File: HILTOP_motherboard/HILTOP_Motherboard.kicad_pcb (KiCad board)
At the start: 4 copper layers, 170 x 170 mm, 709 parts, among them J1 BACKPLANE_PWR, J10 HDMI, J11 DISP_PWR, J12 DISPLAY_PORT, J13 DDR2_SODIMM_COMPUTE_MODULE_3, J14 VADJ_B, J15 VADJ_A, J16 SOFT_START_PWR, J17 PWR_LED, J18 USB_B, J19 Micro_SD_Card, J2 ATX_MOLEX_02X12, J20 CAMERA_PORT, J21 EXT_FAN, J22 BACKPLANE_LV_PWR, J23 EXT_FAN, J24 HILTOP_PCIE-64_CONN, J25 DEBUG, J3 SATA, J4 USB_A_DOUBLE, J5 USB Front Panel, J6 Conn_02x05_Odd_Even, J7 Conn_02x08_Odd_Even, J8 EXT_TEMP_MON, J9 RJ45-TRANS_SI-61001-F, Q1 Q_NMOS_DS_POWERPAK, Q2 Q_NMOS_DS_POWERPAK, Q3 2N7002, Q4 2N7002, Q5 ZXMN6A07F, Q6 ZXMN6A07F, U1 LM337BD2TG, U10 TLC271, U11 ADS1015, U12 MCP4725, U13 AM1S-0505SZ, U14 SP3003-02XJ, U15 ISO3080, U16 ISO3080, U17 AM1S-0505SZ, U18 USB6B1, U19 USB6B1, U2 MIC2026-1YM, U20 USB6B1, U21 USB6B1, U22 BQ32000, U23 TPD12S016, U24 MAX16054, U25 STM6719SFWB6F, U26 LM75B, U27 TPS54394, U28 LP2985, U29 AM1S-0505SZ, U3 USB2517, U30 MCP2517FD, U31 MCP2517FD, U32 AM1S-0505SZ, U33 ADuM1201, U34 ADuM1201, U35 MCP2561FD, U36 MCP2561FD, U37 TUSB9261, U38 AT25DN512CSSHF-B, U39 MCP23017, U4 MIC2026-1YM, U40 SP3003-02XJ, U41 CP2102N-A01-GQFN24, U42 FDC6330L, U43 MAX3107, U44 MAX3107, U45 93AAxxA, U5 SP3003-02XJ, U6 SP3003-02XJ, U7 LAN7500, U8 LM5118, U9 INA250A3, Y1 24MHz Crystal, Y2 25MHz Crystal, Y3 0.22F, Y4 32.768kHz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

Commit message: BOM nearly complete!
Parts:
- removed D66, D67, D69, D70, D71, D72, D73, D77, D78, D79, D80, D81, D82, D83: BAV99, Package_TO_SOT_SMD:SOT-23
- removed R184, R185, R186, R187, R188, R192, R193, R194, R195, R196, R197, R198: 220R, Resistor_SMD:R_0603_1608Metric
- removed R206, R207: 2K2, Resistor_SMD:R_0603_1608Metric
- added D34: BAV99, Package_TO_SOT_SMD:SOT-23, B.Cu at (179.7, 104.2)
- added D35: BAV99, Package_TO_SOT_SMD:SOT-23, B.Cu at (181.6, 100.5)
- added D93: BAV99, Package_TO_SOT_SMD:SOT-23, B.Cu at (176.0, 104.2)
- added D94: BAV99, Package_TO_SOT_SMD:SOT-23, B.Cu at (172.2, 104.2)
- added D95: BAV99, Package_TO_SOT_SMD:SOT-23, B.Cu at (174.1, 100.5)
- added D96: BAV99, Package_TO_SOT_SMD:SOT-23, B.Cu at (177.8, 100.5)
- added J26: Conn_02x06_Odd_Even, Connector_IDC:IDC-Header_2x06_P2.54mm_Vertical, F.Cu at (187.2, 126.8)
- added R245: 220R, Resistor_SMD:R_0402_1005Metric, B.Cu at (181.6, 107.5)
- added R246: 220R, Resistor_SMD:R_0402_1005Metric, B.Cu at (179.9, 107.6)
- added R247: 220R, Resistor_SMD:R_0402_1005Metric, B.Cu at (178.1, 107.8)
- added R248: 220R, Resistor_SMD:R_0402_1005Metric, B.Cu at (176.3, 108.3)
- added R249: 220R, Resistor_SMD:R_0402_1005Metric, B.Cu at (174.1, 108.2)
- added TP17: TP, TestPoint:TestPoint_THTPad_D1.0mm_Drill0.5mm, F.Cu at (232.5, 176.9)
- added TP18: TP, TestPoint:TestPoint_THTPad_D1.0mm_Drill0.5mm, F.Cu at (228.4, 168.7)
- added TP19: TP, TestPoint:TestPoint_THTPad_D1.0mm_Drill0.5mm, F.Cu at (230.5, 166.6)
- added TP20: TP, TestPoint:TestPoint_THTPad_D1.0mm_Drill0.5mm, F.Cu at (228.4, 170.7)
- added TP21: TP, TestPoint:TestPoint_THTPad_D1.0mm_Drill0.5mm, F.Cu at (230.5, 168.7)
- added TP22: TP, TestPoint:TestPoint_THTPad_D1.0mm_Drill0.5mm, F.Cu at (232.5, 166.6)
- added TP23: TP, TestPoint:TestPoint_THTPad_D1.0mm_Drill0.5mm, F.Cu at (228.4, 172.8)
- added TP24: TP, TestPoint:TestPoint_THTPad_D1.0mm_Drill0.5mm, F.Cu at (230.5, 170.7)
- added TP25: TP, TestPoint:TestPoint_THTPad_D1.0mm_Drill0.5mm, F.Cu at (232.5, 168.7)
- added TP26: TP, TestPoint:TestPoint_THTPad_D1.0mm_Drill0.5mm, F.Cu at (234.6, 166.6)
- added TP27: TP, TestPoint:TestPoint_THTPad_D1.0mm_Drill0.5mm, F.Cu at (234.6, 174.8)
- added TP28: TP, TestPoint:TestPoint_THTPad_D1.0mm_Drill0.5mm, F.Cu at (230.5, 172.8)
- added TP29: TP, TestPoint:TestPoint_THTPad_D1.0mm_Drill0.5mm, F.Cu at (232.5, 170.7)
- added TP30: TP, TestPoint:TestPoint_THTPad_D1.0mm_Drill0.5mm, F.Cu at (234.6, 168.7)
- added TP31: TP, TestPoint:TestPoint_THTPad_D1.0mm_Drill0.5mm, F.Cu at (236.6, 166.6)
- added TP32: TP, TestPoint:TestPoint_THTPad_D1.0mm_Drill0.5mm, F.Cu at (228.4, 176.9)
- added TP33: TP, TestPoint:TestPoint_THTPad_D1.0mm_Drill0.5mm, F.Cu at (230.5, 174.8)
- added TP34: TP, TestPoint:TestPoint_THTPad_D1.0mm_Drill0.5mm, F.Cu at (232.5, 172.8)
- added TP35: TP, TestPoint:TestPoint_THTPad_D1.0mm_Drill0.5mm, F.Cu at (234.6, 170.7)
- added TP36: TP, TestPoint:TestPoint_THTPad_D1.0mm_Drill0.5mm, F.Cu at (236.6, 168.7)
- added TP37: TP, TestPoint:TestPoint_THTPad_D1.0mm_Drill0.5mm, F.Cu at (228.4, 166.6)
- added TP38: TP, TestPoint:TestPoint_THTPad_D1.0mm_Drill0.5mm, F.Cu at (228.4, 178.9)
- added TP39: TP, TestPoint:TestPoint_THTPad_D1.0mm_Drill0.5mm, F.Cu at (230.5, 176.9)
- added TP40: TP, TestPoint:TestPoint_THTPad_D1.0mm_Drill0.5mm, F.Cu at (232.5, 174.8)
- added TP41: TP, TestPoint:TestPoint_THTPad_D1.0mm_Drill0.5mm, F.Cu at (234.6, 172.8)
- added TP42: TP, TestPoint:TestPoint_THTPad_D1.0mm_Drill0.5mm, F.Cu at (236.6, 170.7)
- added TP43: TP, TestPoint:TestPoint_THTPad_D1.0mm_Drill0.5mm, F.Cu at (238.7, 168.7)
- added TP44: TP, TestPoint:TestPoint_THTPad_D1.0mm_Drill0.5mm, F.Cu at (240.7, 166.6)
- added TP45: TP, TestPoint:TestPoint_THTPad_D1.0mm_Drill0.5mm, F.Cu at (230.5, 178.9)
- added TP46: TP, TestPoint:TestPoint_THTPad_D1.0mm_Drill0.5mm, F.Cu at (228.4, 174.8)
- added TP47: TP, TestPoint:TestPoint_THTPad_D1.0mm_Drill0.5mm, F.Cu at (238.7, 166.6)
- added TP48: TP, TestPoint:TestPoint_THTPad_D1.0mm_Drill0.5mm, F.Cu at (236.6, 172.8)
- added TP49: TP, TestPoint:TestPoint_THTPad_D1.0mm_Drill0.5mm, F.Cu at (238.7, 170.7)
- added TP50: TP, TestPoint:TestPoint_THTPad_D1.0mm_Drill0.5mm, F.Cu at (240.7, 168.7)
- added TP51: TP, TestPoint:TestPoint_THTPad_D1.0mm_Drill0.5mm, F.Cu at (242.8, 166.6)
- added TP52: TP, TestPoint:TestPoint_THTPad_D1.0mm_Drill0.5mm, F.Cu at (232.5, 178.9)
- added TP53: TP, TestPoint:TestPoint_THTPad_D1.0mm_Drill0.5mm, F.Cu at (234.6, 176.9)
- added TP54: TP, TestPoint:TestPoint_THTPad_D1.0mm_Drill0.5mm, F.Cu at (236.6, 174.8)
- added TP55: TP, TestPoint:TestPoint_THTPad_D1.0mm_Drill0.5mm, F.Cu at (238.7, 172.8)
- added TP56: TP, TestPoint:TestPoint_THTPad_D1.0mm_Drill0.5mm, F.Cu at (251.0, 168.7)
- added TP57: TP, TestPoint:TestPoint_THTPad_D1.0mm_Drill0.5mm, F.Cu at (242.8, 168.7)
- added TP58: TP, TestPoint:TestPoint_THTPad_D1.0mm_Drill0.5mm, F.Cu at (244.8, 166.6)
- added TP59: TP, TestPoint:TestPoint_THTPad_D1.0mm_Drill0.5mm, F.Cu at (234.6, 178.9)
- added TP60: TP, TestPoint:TestPoint_THTPad_D1.0mm_Drill0.5mm, F.Cu at (236.6, 176.9)
- added TP61: TP, TestPoint:TestPoint_THTPad_D1.0mm_Drill0.5mm, F.Cu at (238.7, 174.8)
- added TP62: TP, TestPoint:TestPoint_THTPad_D1.0mm_Drill0.5mm, F.Cu at (240.7, 172.8)
- added TP63: TP, TestPoint:TestPoint_THTPad_D1.0mm_Drill0.5mm, F.Cu at (242.8, 170.7)
- added TP64: TP, TestPoint:TestPoint_THTPad_D1.0mm_Drill0.5mm, F.Cu at (244.8, 168.7)
- added TP65: TP, TestPoint:TestPoint_THTPad_D1.0mm_Drill0.5mm, F.Cu at (246.9, 166.6)
- added TP66: TP, TestPoint:TestPoint_THTPad_D1.0mm_Drill0.5mm, F.Cu at (242.8, 178.9)
- added TP67: TP, TestPoint:TestPoint_THTPad_D1.0mm_Drill0.5mm, F.Cu at (238.7, 176.9)
- added TP68: TP, TestPoint:TestPoint_THTPad_D1.0mm_Drill0.5mm, F.Cu at (240.7, 174.8)
- added TP69: TP, TestPoint:TestPoint_THTPad_D1.0mm_Drill0.5mm, F.Cu at (242.8, 172.8)
- added TP70: TP, TestPoint:TestPoint_THTPad_D1.0mm_Drill0.5mm, F.Cu at (244.8, 170.7)
- added TP71: TP, TestPoint:TestPoint_THTPad_D1.0mm_Drill0.5mm, F.Cu at (246.9, 168.7)
- added TP72: TP, TestPoint:TestPoint_THTPad_D1.0mm_Drill0.5mm, F.Cu at (248.9, 166.6)
- added TP73: TP, TestPoint:TestPoint_THTPad_D1.0mm_Drill0.5mm, F.Cu at (238.7, 178.9)
- added TP74: TP, TestPoint:TestPoint_THTPad_D1.0mm_Drill0.5mm, F.Cu at (240.7, 176.9)
- added TP75: TP, TestPoint:TestPoint_THTPad_D1.0mm_Drill0.5mm, F.Cu at (242.8, 174.8)
- added TP76: TP, TestPoint:TestPoint_THTPad_D1.0mm_Drill0.5mm, F.Cu at (240.7, 170.7)
- added TP77: TP, TestPoint:TestPoint_THTPad_D1.0mm_Drill0.5mm, F.Cu at (246.9, 170.7)
- added TP78: TP, TestPoint:TestPoint_THTPad_D1.0mm_Drill0.5mm, F.Cu at (248.9, 168.7)
- added TP79: TP, TestPoint:TestPoint_THTPad_D1.0mm_Drill0.5mm, F.Cu at (251.0, 166.6)
- added TP80: TP, TestPoint:TestPoint_THTPad_D1.0mm_Drill0.5mm, F.Cu at (240.7, 178.9)
- added TP81: TP, TestPoint:TestPoint_THTPad_D1.0mm_Drill0.5mm, F.Cu at (242.8, 176.9)
- added TP82: TP, TestPoint:TestPoint_THTPad_D1.0mm_Drill0.5mm, F.Cu at (244.8, 174.8)
- added TP83: TP, TestPoint:TestPoint_THTPad_D1.0mm_Drill0.5mm, F.Cu at (246.9, 172.8)
- added TP84: TP, TestPoint:TestPoint_THTPad_D1.0mm_Drill0.5mm, F.Cu at (248.9, 170.7)
- added TP85: TP, TestPoint:TestPoint_THTPad_D1.0mm_Drill0.5mm, F.Cu at (236.6, 178.9)
- added TP86: TP, TestPoint:TestPoint_THTPad_D1.0mm_Drill0.5mm, F.Cu at (244.8, 172.8)
- added TP87: TP, TestPoint:TestPoint_THTPad_D1.0mm_Drill0.5mm, F.Cu at (244.8, 176.9)
- added TP88: TP, TestPoint:TestPoint_THTPad_D1.0mm_Drill0.5mm, F.Cu at (246.9, 174.8)
- added TP89: TP, TestPoint:TestPoint_THTPad_D1.0mm_Drill0.5mm, F.Cu at (248.9, 172.8)
- added TP90: TP, TestPoint:TestPoint_THTPad_D1.0mm_Drill0.5mm, F.Cu at (251.0, 170.7)
- added TP91: TP, TestPoint:TestPoint_THTPad_D1.0mm_Drill0.5mm, F.Cu at (244.8, 178.9)
- added TP92: TP, TestPoint:TestPoint_THTPad_D1.0mm_Drill0.5mm, F.Cu at (246.9, 176.9)
- added TP93: TP, TestPoint:TestPoint_THTPad_D1.0mm_Drill0.5mm, F.Cu at (248.9, 174.8)
- added TP94: TP, TestPoint:TestPoint_THTPad_D1.0mm_Drill0.5mm, F.Cu at (251.0, 172.8)
- C113, C222, C223, C77, D38, D39, D40, D41, D84, FB11, FB7, Q5, Q6, R10, R167, R2, R210, R211, R212, R213, R214, R215, R216, R217, R218, R24, R3, R91, U2, U39, U4, U40, U41, U42: moved to B.Cu
- C18: moved to F.Cu
- D11, D12, D13, D14, D15, D16, D17, D2, D3, D4, D85, D86, D87, D88, D89, D90, D91, D92: footprint LED_SMD:LED_0603_1608Metric -> LED_SMD:LED_0402_1005Metric
- EXP1, EXP2, EXP3: footprint Connector_PinHeader_2.54mm:PinHeader_2x20_P2.54mm_Vertical -> Connector_IDC:IDC-Header_2x20_P2.54mm_Vertical
- J12, J20: footprint Devtank_PCB_Lib:DSI_SFW15R-2STE1LF -> Devtank_PCB_Lib:DSI_FCC15W_VERT
- R140, R141, R153, R154, R155, R156, R157, R158, R182, R183, R189, R190, R191, R235, R236, R237, R238, R239, R240, R241, R242, R28, R35, R36, R37, R38, R39, R40, R41, R42, R43, R44, R45, R46, R47, R48, R80, R82, R84, R86, R87, R88, R89, R90, R92, R93, R94, R95, R96, R97: footprint Resistor_SMD:R_0603_1608Metric -> Resistor_SMD:R_0402_1005Metric
- R178, R179, R180, R181: footprint Resistor_SMD:R_0603_1608Metric -> Resistor_SMD:R_0402_1005Metric; moved to B.Cu
- R54: value DNF -> 220R; footprint Resistor_SMD:R_0603_1608Metric -> Resistor_SMD:R_0402_1005Metric; moved to B.Cu
- moved C21 308.8 mm to (243.5, 107.4)
- moved C28 308.8 mm to (246.2, 111.5)
- moved C32 308.8 mm to (246.2, 112.2)
- moved C35 308.8 mm to (250.6, 108.4)
- moved C37 308.8 mm to (246.2, 113.0)
- moved C39 308.8 mm to (244.6, 114.6)
- moved C40 308.8 mm to (250.6, 109.1)
- moved D11 308.8 mm to (231.8, 114.7)
- moved D12 308.8 mm to (231.8, 111.5)
- moved D13 308.8 mm to (228.8, 114.7)
- moved D14 308.8 mm to (240.5, 104.3)
- moved D15 308.8 mm to (228.8, 113.1)
- moved D16 308.8 mm to (237.4, 105.9)
- moved D17 308.8 mm to (237.4, 104.3)
- moved D2 308.8 mm to (234.9, 111.5)
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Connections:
- J13 pad 30: /Processor/GPIO29 -> /SYS_FAN_DC
- J13 pad 34: /Processor/GPIO30 -> /EXT_TEMP_1WIRE
- J13 pad 36: /Processor/GPIO31 -> /BCK_SHUTDOWN
- J13 pad 46: /Processor/GPIO32 -> /FAN_SENSE_2
- J13 pad 48: /Processor/GPIO33 -> /FAN_SENSE_1
- J13 pad 60: /Processor/GPIO37 -> /DC_DC_ENABLE
- J13 pad 64: /Processor/GPIO38 -> /UART_CH1_CS
- J13 pad 66: /Processor/GPIO39 -> /UART_CH2_CS
- J13 pad 70: /Processor/GPIO40 -> /CAN_CH1_CS
- J13 pad 72: /Processor/GPIO41 -> /CAN_CH2_CS
- J13 pad 76: /Processor/GPIO42 -> /MCP23017_INTA
- J13 pad 78: /Processor/GPIO43 -> /MCP23017_INTB
- J13 pad 82: Net-(D66-Pad3) -> /DC_OUT_ENABLE
- J13 pad 84: Net-(D67-Pad3) -> /ATX_PWR_SHDN
- J2 pad 20: Net-(J2-Pad20) -> (no net)
- Q3 pad 1: (no net) -> Net-(Q3-Pad1)
- R100 pad 1: Net-(D67-Pad3) -> /ATX_PWR_SHDN
- R101 pad 1: Net-(D66-Pad3) -> /DC_OUT_ENABLE
- R108 pad 1: Net-(R108-Pad1) -> Net-(Q3-Pad1)
- R110 pad 2: Net-(R108-Pad1) -> Net-(Q3-Pad1)
- R54 pad 1: Net-(C119-Pad2) -> Net-(J26-Pad1)
- R54 pad 2: Net-(J2-Pad20) -> /EXT_GPIO1
- R99 pad 1: /Processor/GPIO29 -> /SYS_FAN_DC
- U30 pad 8: (no net) -> /CAN2_INT1
- U30 pad 9: (no net) -> /CAN2_INT0
- U31 pad 8: (no net) -> /CAN1_INT1
- U31 pad 9: (no net) -> /CAN1_INT0
- U39 pad 23: (no net) -> /EXT_GPIO1
- U39 pad 24: (no net) -> /EXT_GPIO2
- U39 pad 25: (no net) -> /EXT_GPIO3
- U39 pad 26: (no net) -> /EXT_GPIO4
- U39 pad 27: (no net) -> /EXT_GPIO5
- U39 pad 28: (no net) -> /EXT_GPIO6
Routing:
- net +1V8: track 124.2 -> 36.5 mm, vias 2 -> 1
- net Net-(J2-Pad20): track 33.2 -> 0.00 mm
- net +CM_1V8: track 40.3 -> 21.2 mm
- net /AdjPower/VADJ_DC: track 0.00 -> 17.2 mm
- net ADJ_DC: track 0.00 -> 15.2 mm
- net Net-(C113-Pad1): track 15.0 -> 0.90 mm
- net /Processor/HDMI_SDA: track 18.0 -> 5.82 mm, vias 1 -> 0
- net /Processor/HDMI_HPD: track 17.7 -> 5.71 mm
- net /Processor/GPIO4: track 9.29 -> 0.00 mm, vias 1 -> 0
- net /Processor/SDX_D2: track 27.9 -> 19.2 mm
- net /Processor/SDX_D0: track 27.5 -> 19.0 mm, vias 2 -> 0
- net /Processor/SDX_D1: track 27.2 -> 18.6 mm, vias 2 -> 0
- net /Processor/SDX_CLK: track 27.5 -> 19.0 mm
- net /Processor/SDX_D3: track 27.4 -> 18.9 mm, vias 2 -> 0
- net /Processor/SDX_CMD: track 27.5 -> 19.7 mm
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- added copper zone on F.Cu, net Net-(C50-Pad2)
- removed copper zone on In2.Cu, net ADJ_DC
- removed copper zone on In1.Cu, net GND
- removed copper zone on In2.Cu, net GND_ISO4
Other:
- copper layers 4 -> 6

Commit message: nearly finished placing all parts!
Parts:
- removed C53, C55: 100nF, Capacitor_SMD:C_0201_0603Metric
- removed C59, C71, C72, C73: 100nF, Capacitor_SMD:C_0603_1608Metric
- removed D52, D53: BAV99, Package_TO_SOT_SMD:SOT-23
- removed EXP3: CONN_02X20, Connector_IDC:IDC-Header_2x20_P2.54mm_Vertical
- removed R210, R213: 100K, Resistor_SMD:R_0603_1608Metric
- removed R211: DNP, Resistor_SMD:R_0603_1608Metric
- removed R212, R214: 1K, Resistor_SMD:R_0603_1608Metric
- removed R93, R94: 220R, Resistor_SMD:R_0402_1005Metric
- removed U42: FDC6330L, Devtank_PCB_Lib:SuperSOT-6
- removed W1: TP, TestPoint:TestPoint_THTPad_1.5x1.5mm_Drill0.7mm
- removed Y3: 0.22F, Devtank_PCB_Lib:Battery_SD_V_SuperCap
- added BT1: Battery_Cell, Devtank_PCB_Lib:BatteryHolder_Keystone_1061_1x20mm, F.Cu at (155.1, 155.9)
- added C237: DNF, Capacitor_SMD:C_0603_1608Metric, F.Cu at (211.9, 89.5)
- added C238: DNF, Capacitor_SMD:C_0603_1608Metric, F.Cu at (215.7, 92.8)
- added D66: MBR230LSFT, Diode_SMD:D_SOD-123F, F.Cu at (154.2, 157.8)
- added Q7: ZXMN6A07F, Package_TO_SOT_SMD:SOT-23, F.Cu at (206.2, 88.9)
- added Q8: SSM3J328R, Package_TO_SOT_SMD:SOT-23, F.Cu at (211.8, 94.8)
- added R184: 10K, Resistor_SMD:R_0603_1608Metric, F.Cu at (211.9, 91.7)
- added R185: 10K, Resistor_SMD:R_0603_1608Metric, F.Cu at (206.3, 85.0)
- added TP95: TP, TestPoint:TestPoint_THTPad_D1.0mm_Drill0.5mm, F.Cu at (197.4, 178.2)
- C100, C101, C102, C15, C153, C154, C181, C182, C183, C195, C196, C20, C201, C202, C203, C205, C207, C209, C211, C212, C213, C214, C215, C216, C217, C218, C220, C221, C224, C43, C45, C46, C65, C76, C84, D42, D43, D44, D45, D46, D47, D48, D49, D50, D51, D54, D55, D59, D60, D61, D62, D63, D64, D65, R11, R18, R182, R19: moved to B.Cu
- C197, C198, C199, C200: footprint Resistor_SMD:R_0402_1005Metric -> Capacitor_SMD:C_0402_1005Metric
- C47, C48, C49: footprint Resistor_SMD:R_0603_1608Metric -> Capacitor_SMD:C_0603_1608Metric
- D1, D21, D22, D23: value Green_LED -> GRN; footprint LED_SMD:LED_0603_1608Metric -> LED_SMD:LED_0402_1005Metric
- D18: value Green_LED -> GRN; footprint LEDs:LED_0603 -> LED_SMD:LED_0402_1005Metric
- D25, D26, D27, D28, D29, D30, D31, D32, D33: footprint LED_SMD:LED_0603_1608Metric -> LED_SMD:LED_0402_1005Metric
- D84, R167, U41: moved to F.Cu
- F1: value PPTC 2A, 3.8A, 32V -> PPTC 3.8A
- J26: value Conn_02x06_Odd_Even -> IO_EXP
- J5: value USB Front Panel -> USB FRONT PANEL
- J6: value Conn_02x05_Odd_Even -> CAN
- J7: value Conn_02x08_Odd_Even -> RS485
- L11, L5, L6, L7: value 15uH -> 10uH
- Q1, Q2: value Q_NMOS_DS_POWERPAK -> Si7148DP-T1-E3
- R100, R101, R102, R31, R32, R33, R99: footprint Resistor_SMD:R_0603_1608Metric -> Resistor_SMD:R_0402_1005Metric
- R159: value 0R -> 10K
- TP15, TP16: value Test_Point -> TP
- U13, U17, U29, U32: value AM1S-0505SZ -> CME0505S3C
- U39: footprint Package_SO:SOIC-28W_7.5x17.9mm_P1.27mm -> Package_SO:SSOP-28_5.3x10.2mm_P0.65mm
- moved R95 240.5 mm to (191.8, 102.2), turned to 270 degrees
- moved R97 236.5 mm to (190.4, 102.2), turned to 270 degrees
- moved R92 235.6 mm to (195.0, 95.8)
- moved C224 231.0 mm to (182.3, 65.5)
- moved R96 228.8 mm to (189.0, 102.2), turned to 90 degrees
- moved C225 228.7 mm to (183.2, 65.4)
- moved C217 227.2 mm to (178.5, 66.5), turned to 180 degrees
- moved R140 227.0 mm to (187.6, 102.2), turned to 270 degrees
- moved R141 225.7 mm to (182.0, 102.2), turned to 270 degrees
- moved R86 224.5 mm to (183.4, 102.2), turned to 270 degrees
- moved R156 223.9 mm to (171.3, 102.2), turned to 270 degrees
- moved R153 223.3 mm to (186.2, 102.2), turned to 90 degrees
- moved R84 223.0 mm to (184.8, 102.2), turned to 270 degrees
- moved R87 222.7 mm to (179.2, 102.2), turned to 270 degrees
- moved C219 221.1 mm to (178.8, 67.0), turned to 180 degrees
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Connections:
- C102 pad 2: Net-(C102-Pad2) -> +5V
- C15 pad 2: GND -> GND_ISO3
- C20 pad 2: GND -> GND_ISO4
- C44 pad 2: Net-(C44-Pad2) -> +5V
- C78 pad 2: Net-(C78-Pad2) -> +5V
- C84 pad 2: Net-(C84-Pad2) -> +5V
- FL1 pad 1: Net-(C161-Pad1) -> Net-(C158-Pad1)
- FL1 pad 2: /CAN2_H -> Net-(C161-Pad1)
- FL1 pad 3: Net-(C158-Pad1) -> /CAN2_H
- FL2 pad 1: Net-(C162-Pad1) -> Net-(C159-Pad1)
- FL2 pad 2: /CAN1_H -> Net-(C162-Pad1)
- FL2 pad 3: Net-(C159-Pad1) -> /CAN1_H
- J13 pad 51: /Processor/GPIO14 -> /DEBUG_TX
- J13 pad 53: /Processor/GPIO15 -> /DEBUG_RX
- L11 pad 1: +5V -> Net-(L11-Pad1)
- L11 pad 2: Net-(C102-Pad2) -> +5V_ISO2
- L5 pad 1: +5V -> Net-(L5-Pad1)
- L5 pad 2: Net-(C78-Pad2) -> +5V_ISO3
- L6 pad 1: +5V -> Net-(L6-Pad1)
- L6 pad 2: Net-(C44-Pad2) -> +5V_ISO4
- L7 pad 1: +5V -> Net-(L7-Pad1)
- L7 pad 2: Net-(C84-Pad2) -> +5V_ISO1
- R159 pad 1: Net-(R159-Pad1) -> /SYS_FAN_DC
- R159 pad 2: Net-(R159-Pad2) -> GND
- TP35 pad 1: /CAN1_INT -> GND
- TP36 pad 1: /CAN1_INT0 -> GND
- TP37 pad 1: /CAN1_INT1 -> GND
- TP40 pad 1: /CAN2_INT -> GND
- TP41 pad 1: /CAN2_INT0 -> GND
- TP42 pad 1: /CAN2_INT1 -> GND
- U13 pad 2: Net-(C78-Pad2) -> +5V
- U13 pad 4: +5V_ISO3 -> Net-(L5-Pad1)
- U17 pad 2: Net-(C44-Pad2) -> +5V
- U17 pad 4: +5V_ISO4 -> Net-(L6-Pad1)
- U22 pad 3: Net-(R159-Pad1) -> Net-(D66-Pad1)
- U22 pad 5: /Processor/SDA1 -> /I2C1_SDA
- U22 pad 6: /Processor/SCL1 -> /I2C1_SCL
- U26 pad 1: /Processor/SDA1 -> /Processor/SDA_M1
- U26 pad 2: /Processor/SCL1 -> /Processor/SCL_M1
- U29 pad 2: Net-(C84-Pad2) -> +5V
- U29 pad 4: +5V_ISO1 -> Net-(L7-Pad1)
- U30 pad 8: /CAN2_INT1 -> (no net)
- U30 pad 9: /CAN2_INT0 -> (no net)
- U31 pad 8: /CAN1_INT1 -> (no net)
- U31 pad 9: /CAN1_INT0 -> (no net)
- U32 pad 2: Net-(C102-Pad2) -> +5V
- U32 pad 4: +5V_ISO2 -> Net-(L11-Pad1)
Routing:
- net /I2C1_SCL: track 0.00 -> 208.8 mm, vias 0 -> 5
- net /I2C1_SDA: track 0.00 -> 208.5 mm, vias 0 -> 6
- net /CAM1_CK_P: track 0.00 -> 71.4 mm, vias 0 -> 2
- net /CAM1_D0_P: track 0.00 -> 70.1 mm, vias 0 -> 2
- net /CAM1_D1_N: track 0.00 -> 70.1 mm, vias 0 -> 2
- net /CAM1_D1_P: track 0.00 -> 69.1 mm, vias 0 -> 2
- net /CAM1_CK_N: track 0.00 -> 68.8 mm, vias 0 -> 2
- net /CAM1_D0_N: track 0.00 -> 67.6 mm, vias 0 -> 2
- net /DISP1_D0_P: track 0.00 -> 60.3 mm
- net /DISP1_D1_P: track 0.00 -> 60.0 mm
- net /DISP1_CK_N: track 0.00 -> 60.0 mm
- net /DISP1_CK_P: track 0.00 -> 58.5 mm
- net /DISP1_D0_N: track 0.00 -> 57.9 mm
- net /DISP1_D1_N: track 0.00 -> 57.5 mm
- net (no net): track 69.5 -> 21.9 mm
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
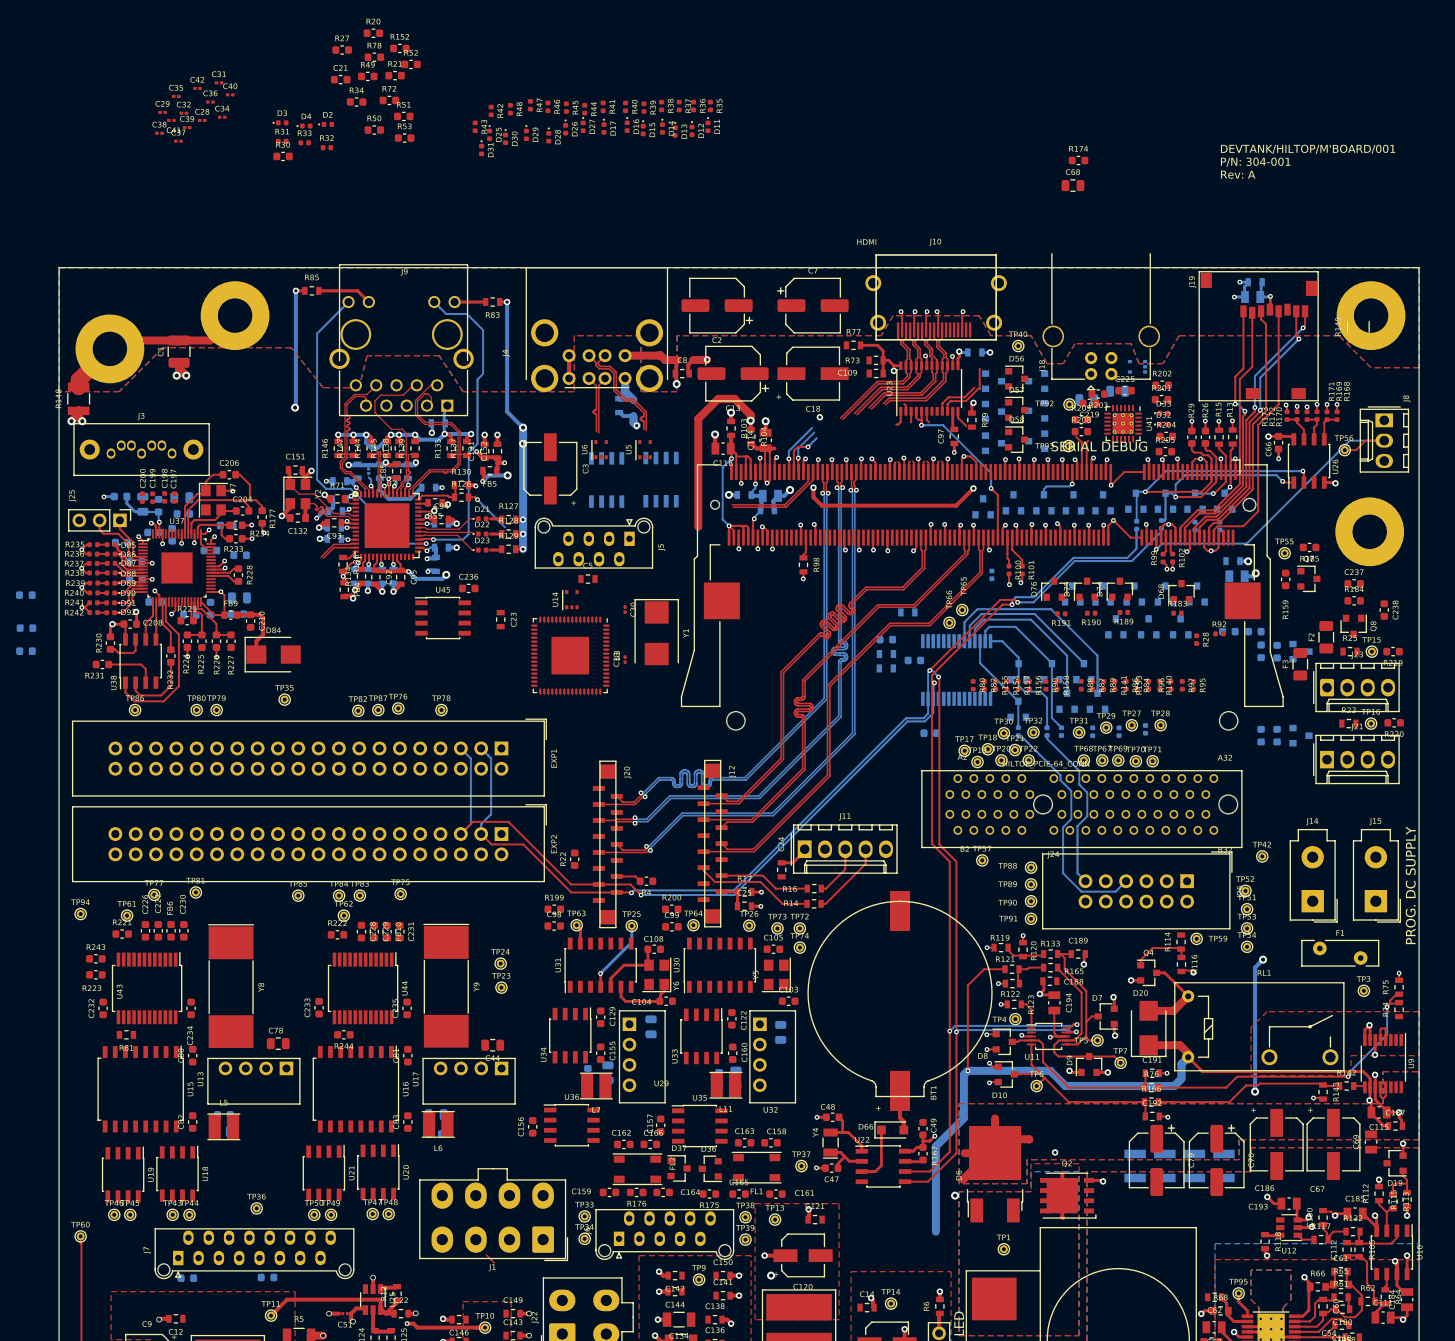
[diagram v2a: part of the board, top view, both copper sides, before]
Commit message: All parts placed and backplane connector checked and locked
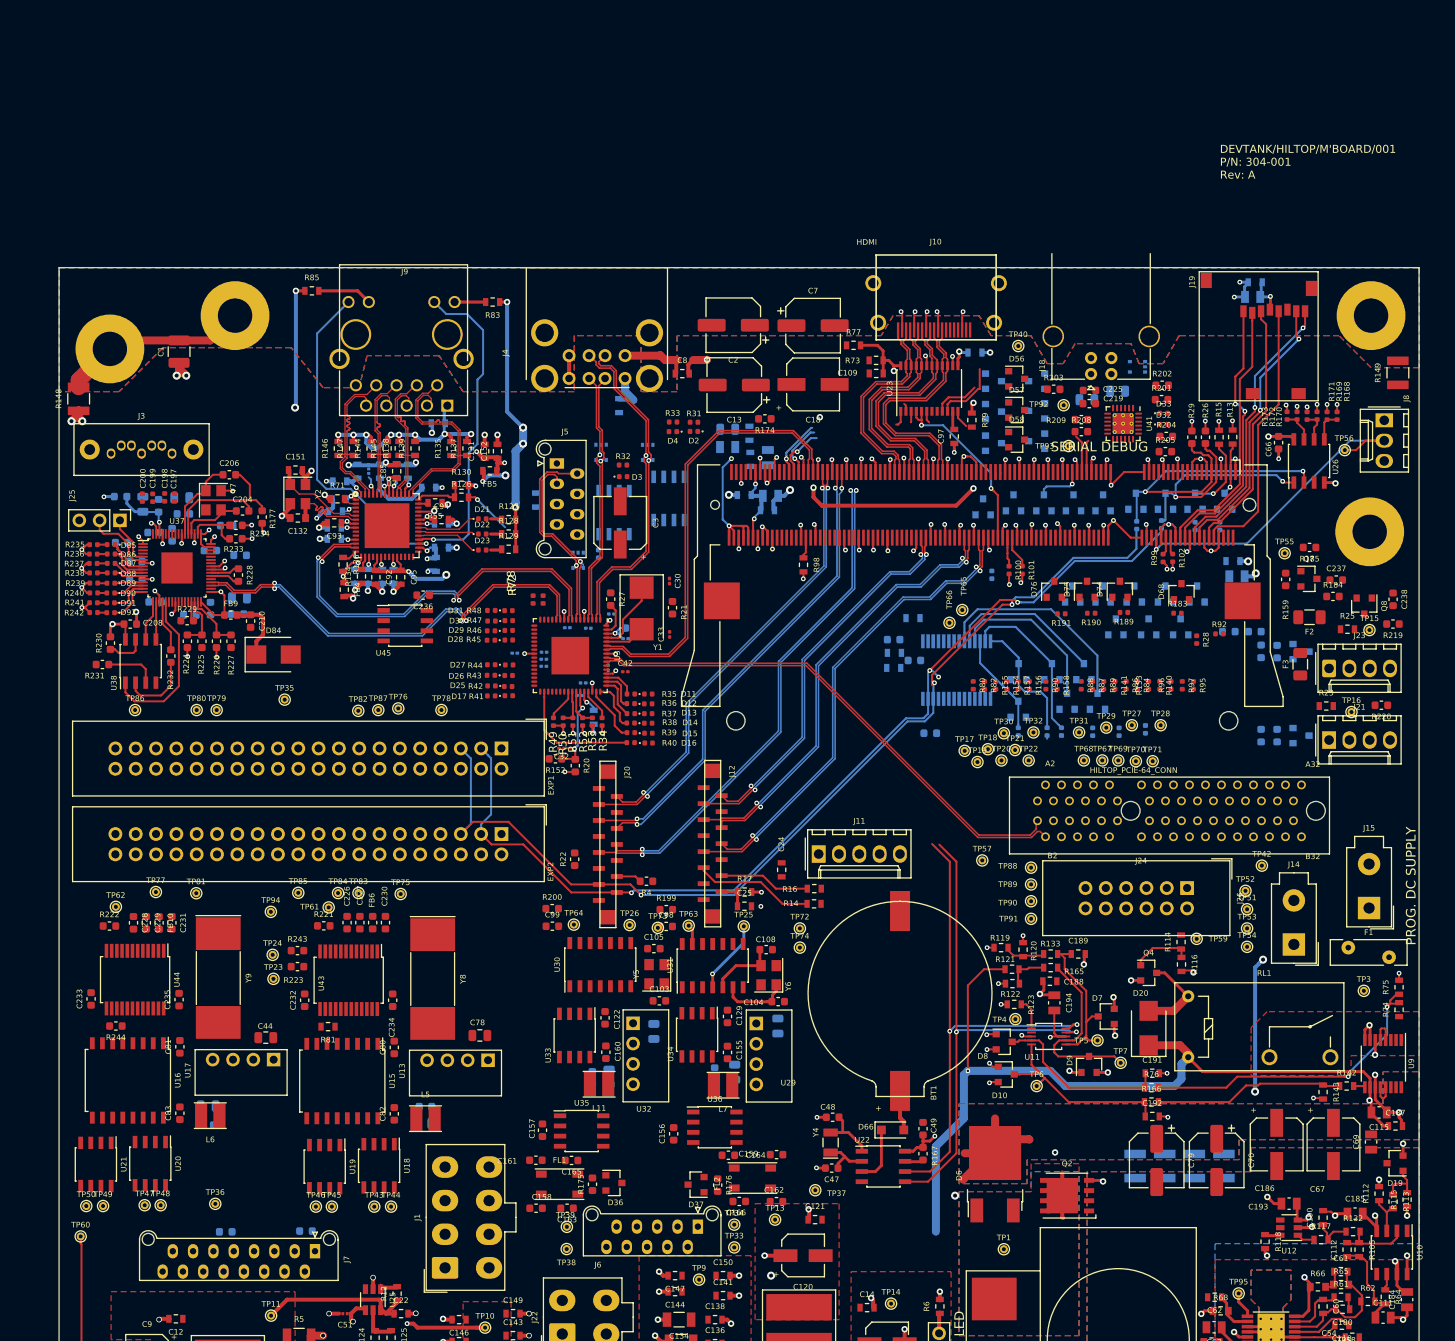
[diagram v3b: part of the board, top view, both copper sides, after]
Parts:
- removed C202, C214, C220: 100nF, Capacitor_SMD:C_0603_1608Metric
- C114, C116, C21, C23, C28, C29, C31, C34, C35, C36, C37, C38, C39, C40, C41, C5, C68, R103, R104, U14, U5, U6: moved to B.Cu
- R30: footprint Resistor_SMD:R_0603_1608Metric -> Resistor_SMD:R_0402_1005Metric; moved to B.Cu
- R34, R49, R50, R51, R52, R53, R72, R78: footprint Resistor_SMD:R_0603_1608Metric -> Resistor_SMD:R_0402_1005Metric
- moved R20 95.0 mm to (114.5, 112.2), turned to 270 degrees
- moved C32 92.4 mm to (112.8, 110.1), turned to 180 degrees
- moved R152 90.9 mm to (112.0, 111.4), turned to 180 degrees
- moved C42 90.4 mm to (120.8, 100.5)
- moved C41 88.1 mm to (115.1, 103.5), turned to 180 degrees
- moved C40 85.8 mm to (118.6, 100.0), turned to 90 degrees
- moved C39 85.2 mm to (115.5, 101.9), turned to 180 degrees
- moved R52 84.9 mm to (115.4, 106.8), turned to 270 degrees
- moved C35 84.8 mm to (110.6, 99.8)
- moved R49 83.9 mm to (111.8, 106.8), turned to 270 degrees
- moved C28 83.6 mm to (120.8, 96.4)
- moved C29 83.3 mm to (110.6, 99.0)
- moved R34 83.3 mm to (117.9, 106.8), turned to 270 degrees
- moved C31 81.9 mm to (110.6, 98.1)
- moved C38 81.9 mm to (116.2, 95.1)
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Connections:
- U3 pad 20: /USBHub/USB4_EN -> (no net)
- U3 pad 21: /USBHub/OCS4 -> (no net)
- U3 pad 22: (no net) -> /USBHub/OCS3
- U3 pad 23: (no net) -> /USBHub/USB3_EN
- U3 pad 6: /LAN_USB_N -> /FR_PANEL_USB_N
- U3 pad 7: /LAN_USB_P -> /FR_PANEL_USB_P
- U3 pad 8: /FR_PANEL_USB_N -> /LAN_USB_N
- U3 pad 9: /FR_PANEL_USB_P -> /LAN_USB_P
- U4 pad 1: /USBHub/USB4_EN -> /USBHub/USB3_EN
- U4 pad 2: /USBHub/OCS4 -> /USBHub/OCS3
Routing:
- net /BACKPLANE_USB_N: track 0.00 -> 64.7 mm
- net /BACKPLANE_USB_P: track 0.00 -> 64.4 mm
- net /SATA_USB_N: track 0.00 -> 55.1 mm, vias 0 -> 2
- net /USBHub/PWR1_5V: track 63.2 -> 8.51 mm, vias 1 -> 0
- net /SATA_USB_P: track 0.00 -> 54.6 mm, vias 0 -> 2
- net /LAN_USB_N: track 5.05 -> 52.2 mm, vias 0 -> 2
- net /USBHub/PWR2_5V: track 51.9 -> 5.00 mm
- net /LAN_USB_P: track 4.59 -> 50.7 mm, vias 0 -> 2
- net /USB_ROOT_N: track 11.9 -> 53.8 mm
- net /USB_ROOT_P: track 12.4 -> 54.3 mm
- net Net-(J26-Pad7): track 29.9 -> 0.00 mm
- net /USBHub/USB1_N: track 13.5 -> 41.5 mm, vias 0 -> 1
- net /USBHub/USB1_P: track 13.9 -> 41.7 mm, vias 0 -> 1
- net /FR_PANEL_USB_P: track 0.00 -> 25.9 mm, vias 0 -> 1
- net /USBHub/USB2_N: track 7.12 -> 32.2 mm, vias 0 -> 1
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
